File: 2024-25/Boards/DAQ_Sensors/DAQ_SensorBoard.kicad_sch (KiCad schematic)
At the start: 7 parts, among them J1 Conn_01x20_Socket, J2 Conn_01x20_Pin, U1 74LS352, U2 LTC1298CN8-PBF

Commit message: update
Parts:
- added R2, R3: 10k, Resistor_SMD:R_0805_2012Metric_Pad1.20x1.40mm_HandSolder, symbol Device:R_US
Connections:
- net +5V: now also R2.1, R3.1
- net Digital_Temp_Out: now also J1.15 (Pin_15), U1.9 (Zb); no longer J1.11 (Pin_11)
- net GND: now also J1.10 (Pin_10), J1.12 (Pin_12), J1.14 (Pin_14)
- net Pressure1_dig: now also U1.5 (I1a), U1.6 (I0a)
- net Pressure2_dig: now also U1.3 (I3a), U1.4 (I2a)
- net Temp_1+: now reaches R1.2
- net Temp_1+: now also J1.9 (Pin_9)
- net Temp_3+: now reaches J1.13 (Pin_13)
- net Temp_3+: now also R3.2
- net Temp1_dig: now reaches U1.10 (I0b)
- net Temp2_dig: now reaches U1.11 (I1b)
- net Temp3_dig: now reaches U1.12 (I2b)
- new net Temp_2+: J1.11 (Pin_11), R2.2
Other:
- note added: "+5V from battery or powerline?"
- note added: "Selection MUX"

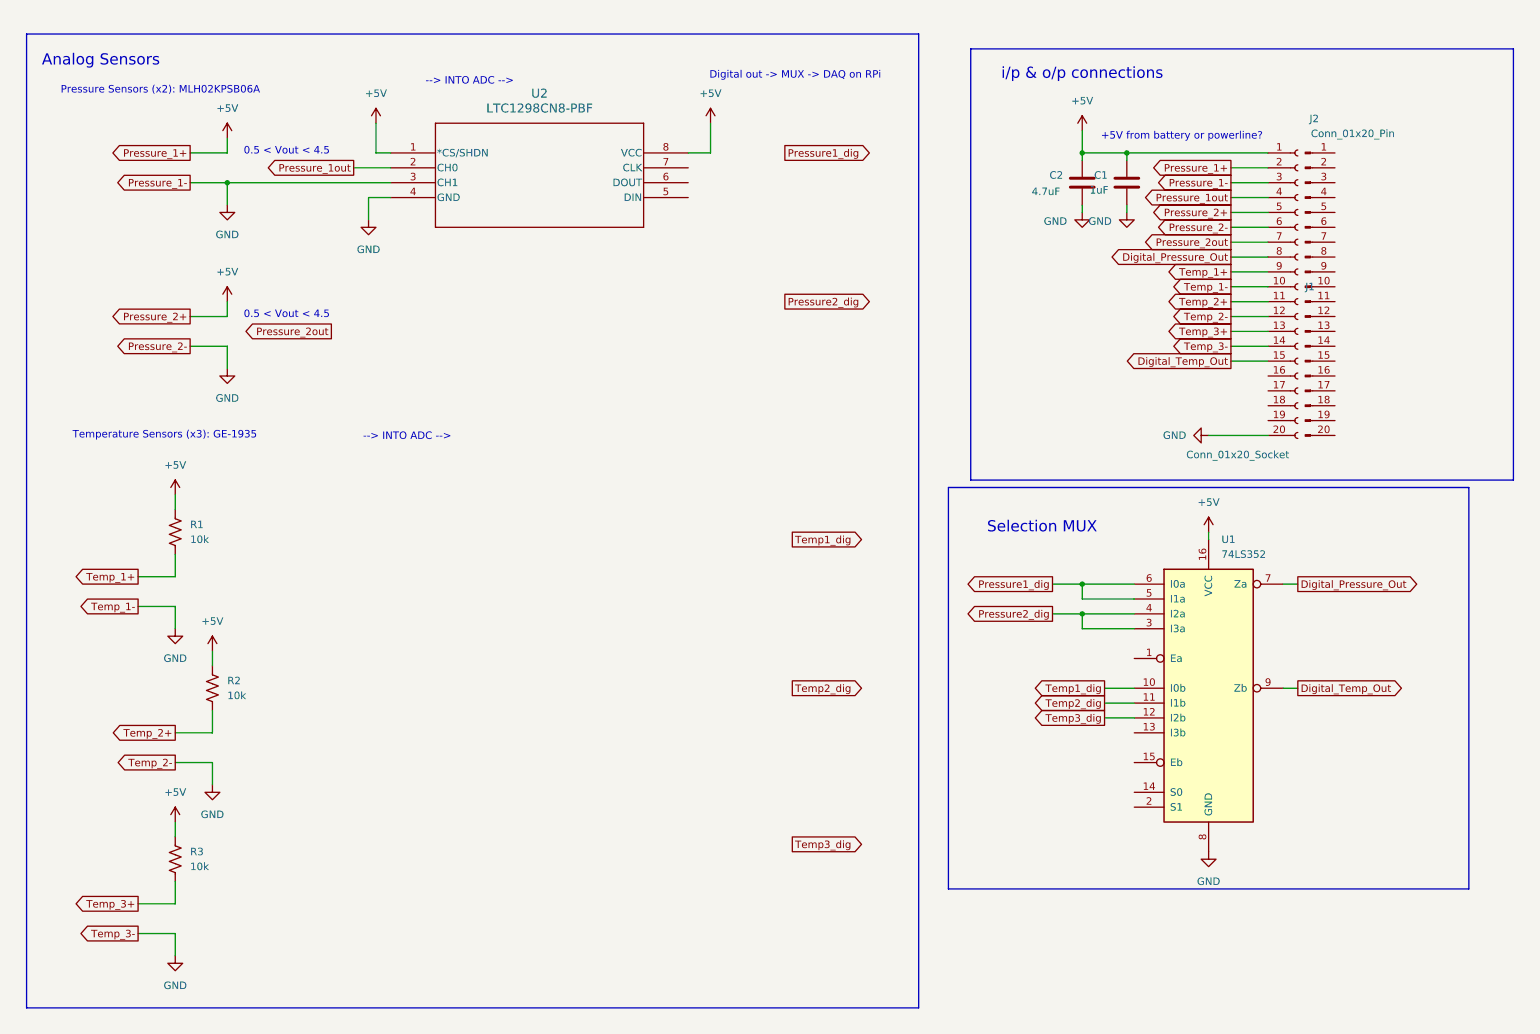
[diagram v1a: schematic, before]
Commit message: changed to 1 ADC with SPI
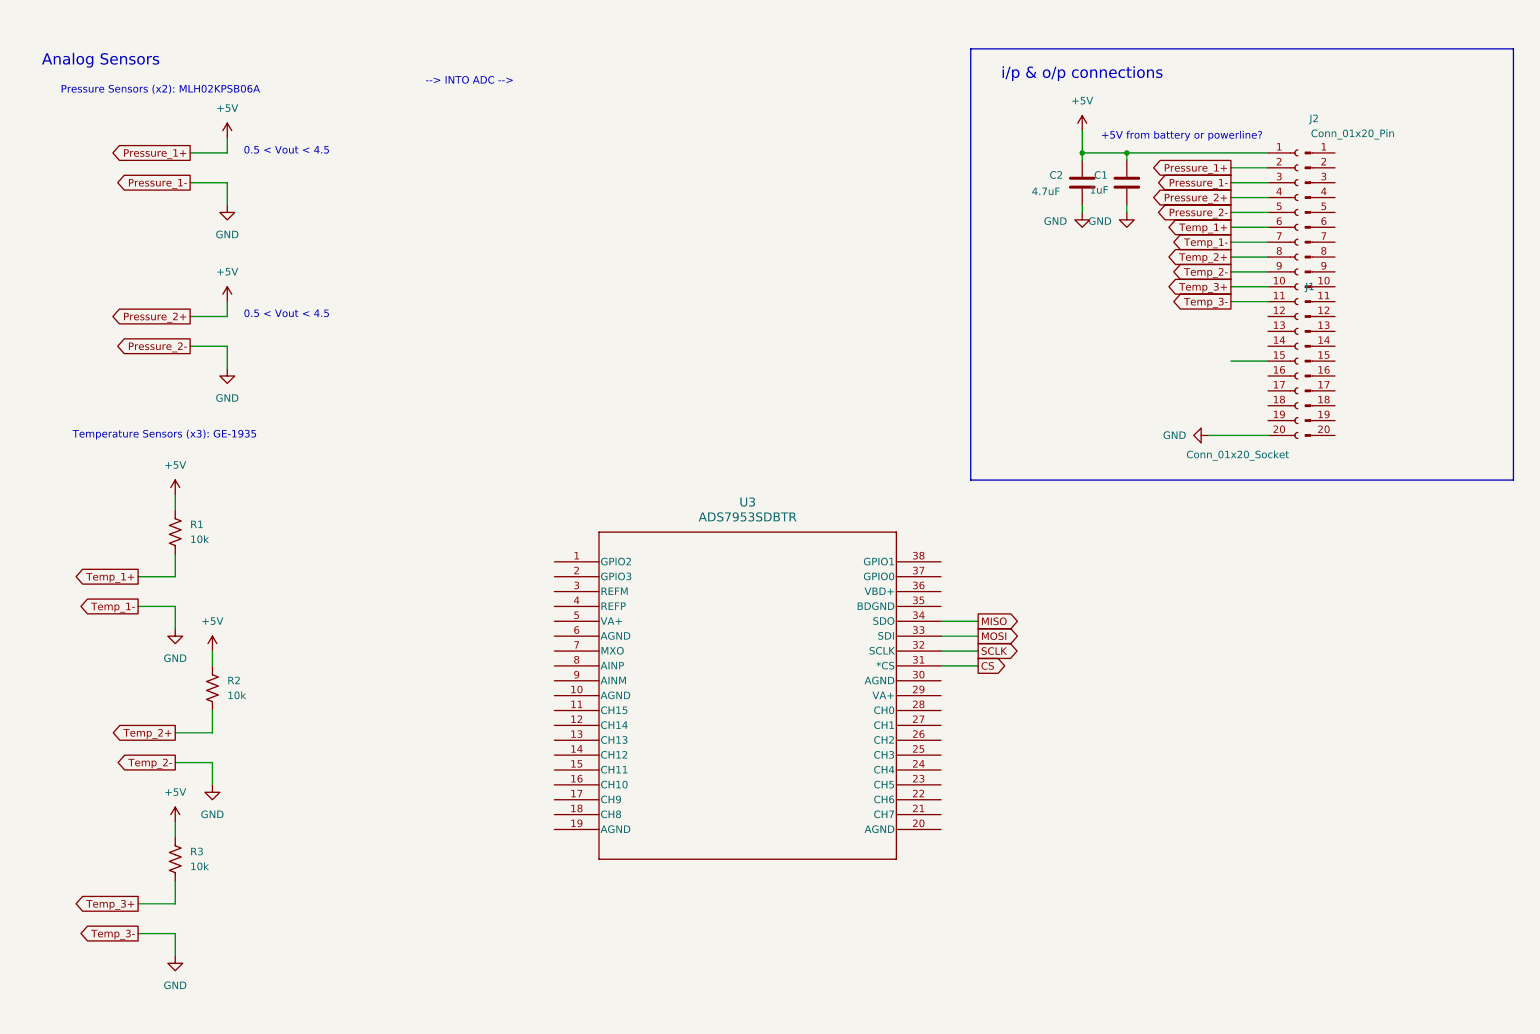
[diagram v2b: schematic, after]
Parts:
- removed U1: 74LS352, symbol 74xx:74LS352
- removed U2: LTC1298CN8-PBF, PDIP-8_N_LIT, symbol LTC1298CN8:LTC1298CN8-PBF
- added U3: ADS7953SDBTR, DBT38, symbol ADS7953SDBTR:ADS7953SDBTR
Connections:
- net Digital_Pressure_Out is gone; now on net Temp_2+: J1.8 (Pin_8)
- net Pressure_1out is gone; now on net +5V: J1.4 (Pin_4)
- net Pressure_2out is gone; now on net GND: J1.7 (Pin_7)
- net +5V: no longer J1.5 (Pin_5)
- net GND: now also J1.11 (Pin_11), J1.5 (Pin_5), J1.9 (Pin_9); no longer J1.10 (Pin_10), J1.12 (Pin_12), J1.14 (Pin_14), J1.6 (Pin_6)
- net Temp_1+: now also J1.6 (Pin_6); no longer J1.9 (Pin_9)
- net Temp_2+: no longer J1.11 (Pin_11)
- net Temp_3+: now also J1.10 (Pin_10); no longer J1.13 (Pin_13)
- net Digital_Temp_Out: no longer names the net of J1.15 (Pin_15)
- new net CS: U3.31 (*CS)
- new net MISO: U3.34 (SDO)
- new net MOSI: U3.33 (SDI)
- new net SCLK: U3.32 (SCLK)
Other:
- note removed: "Digital out -> MUX -> DAQ on RPi"
- note removed: "Selection MUX"

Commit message: completed v1
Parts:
- removed J1: Conn_01x20_Socket, symbol Connector:Conn_01x20_Socket
- removed J2: Conn_01x20_Pin, symbol Connector:Conn_01x20_Pin
- added C3, C4, C5: 1uF, Capacitor_SMD:C_0805_2012Metric_Pad1.18x1.45mm_HandSolder, symbol Device:C
- added J1: Conn_01x24_Pin, symbol Connector:Conn_01x24_Pin
- added J2: Conn_01x24_Socket, symbol Connector:Conn_01x24_Socket
- added TP1: TestPoint, TestPoint:TestPoint_THTPad_2.5x2.5mm_Drill1.2mm, symbol Connector:TestPoint
- added U1, U4: MIC5504-3.3YM5, Package_TO_SOT_SMD:SOT-23-5, symbol Regulator_Linear:MIC5504-3.3YM5
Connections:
- net +5V: now also U3.29 (VA+), U3.5 (VA+), C3.1, C5.1, J2.1 (Pin_1), J2.2 (Pin_2), J2.4 (Pin_4), U1.1 (VIN), U4.1 (VIN)
- net CS: now also J2.17 (Pin_17)
- net GND: now also U3.10 (AGND), U3.19 (AGND), U3.20 (AGND), U3.3 (REFM), U3.30 (AGND), U3.35 (BDGND), U3.6 (AGND), U3.9 (AINM), C3.2, C4.2, C5.2, J2.11 (Pin_11), J2.3 (Pin_3), J2.5 (Pin_5), J2.7 (Pin_7), J2.9 (Pin_9), U1.2 (GND), U4.2 (GND)
- net MISO: now also J2.15 (Pin_15)
- net MOSI: now also J2.14 (Pin_14)
- net SCLK: now also J2.16 (Pin_16)
- net Temp_1+: now also U3.26 (CH2), J2.6 (Pin_6)
- net Temp_2+: now also U3.25 (CH3), J2.8 (Pin_8)
- net Temp_3+: now also U3.24 (CH4), J2.10 (Pin_10)
- net GPIO2: now reaches U3.1 (GPIO2)
- net GPIO2: now also J2.20 (Pin_20)
- net GPIO3: now reaches U3.2 (GPIO3)
- net GPIO3: now also J2.21 (Pin_21)
- net Pressure2_out: now reaches U3.27 (CH1)
- net Pressure2_out: now also J2.13 (Pin_13)
- net Pressure1_out: now reaches U3.28 (CH0)
- net Pressure1_out: now also J2.12 (Pin_12)
- net +3.3V: now reaches U3.36 (VBD+)
- net +3.3V: now also C4.1, U1.5 (VOUT)
- net GPIO0: now reaches U3.37 (GPIO0)
- net GPIO0: now also J2.18 (Pin_18)
- net GPIO1: now reaches U3.38 (GPIO1)
- net GPIO1: now also J2.19 (Pin_19)
- net +2.5V: now reaches U3.4 (REFP)
- net +2.5V: now also U4.5 (VOUT)
- net at U3.7 (MXO): now also U3.8 (AINP), TP1.1
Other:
- note added: "(unsure of where to route enable pins on LDOs)"
- note added: "ADC to Teensy"
- note added: "ADC: Sensor data -> SPI"
- note added: "ENABLE?"
- note added: "Voltage Regulators"
- note added: "from channel mux to ADC"
- note removed: "--> INTO ADC -->"
- moved on the sheet: C1, C2, U3

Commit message: small changes to docu
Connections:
- net +3.3V: now also C5.1, U4.1 (VIN)
- net +5V: no longer C5.1, U4.1 (VIN)
- net GND: now also J2.24 (Pin_24)
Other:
- note added: "ADC (SPI to Teensy)"
- note added: "note: internal enable pulldown in both LDOs"
- note removed: "(unsure of where to route enable pins on LDOs)"
- note removed: "ADC to Teensy"
- note removed: "ENABLE?"
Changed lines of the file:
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@@
 	(wire
 		(pts
+			(xy 220.98 91.44) (xy 234.95 91.44)
+		)
+		(stroke
+			(width 0)
+			(type default)
+		)
+	)
+	(wire
+		(pts
 			(xy 111.76 132.08) (xy 111.76 154.94)
 		)
@@
 		)
 	)
-	(text "(unsure of where to route enable pins on LDOs)"
+	(text "note: internal enable pulldown in both LDOs"
 		(exclude_from_sim no)
-		(at 129.032 26.67 0)
-		(effects
-			(font
-				(size 1.27 1.27)
-			)
-		)
-	)
-	(text "ENABLE?"
-		(exclude_from_sim no)
-		(at 94.234 60.452 0)
+		(at 156.718 81.788 0)
 		(effects
 			(font
@@
 		)
 	)
-	(text "ENABLE?"
-		(exclude_from_sim no)
-		(at 150.114 57.912 0)
-		(effects
-			(font
-				(size 1.27 1.27)
-			)
-		)
-	)
 	(text "Temperature Sensors (x3): GE-1935"
 		(exclude_from_sim no)
@@
 		)
 	)
-	(text "ADC to Teensy"
+	(text "ADC (SPI to Teensy)"
 		(exclude_from_sim no)
 		(at 100.33 92.964 0)
@@
 		(on_board yes)
 		(dnp no)
-		(fields_autoplaced yes)
 		(property "Reference" "J2"
 			(at 241.3 60.9599 0)
@@
 		)
 		(property "Value" "Conn_01x24_Socket"
-			(at 241.3 63.4999 0)
+			(at 249.936 68.834 0)
 			(effects
 				(font
@@
 	(symbol
 		(lib_id "power:GND")
-		(at 207.01 86.36 270)
+		(at 220.98 91.44 270)
 		(unit 1)
 		(exclude_from_sim no)
@@
 		(fields_autoplaced yes)
 		(property "Reference" "#PWR03"
-			(at 200.66 86.36 0)
+			(at 214.63 91.44 0)
 			(effects
 				(font
@@
 		)
 		(property "Value" "GND"
-			(at 203.2 86.3599 90)
+			(at 217.17 91.4399 90)
 			(effects
 				(font
@@
 		)
 		(property "Footprint" ""
-			(at 207.01 86.36 0)
+			(at 220.98 91.44 0)
 			(effects
 				(font
@@
 		)
 		(property "Datasheet" ""
-			(at 207.01 86.36 0)
+			(at 220.98 91.44 0)
 			(effects
 				(font
@@
 		)
 		(property "Description" "Power symbol creates a global label with name \"GND\" , ground"
-			(at 207.01 86.36 0)
+			(at 220.98 91.44 0)
 			(effects
 				(font
@@
 	(symbol
 		(lib_id "power:+3.3V")
-		(at 124.46 53.34 270)
+		(at 86.36 39.37 0)
 		(unit 1)
 		(exclude_from_sim no)
@@
 		(on_board yes)
 		(dnp no)
-		(property "Reference" "#PWR026"
-			(at 120.65 53.34 0)
+		(fields_autoplaced yes)
+		(property "Reference" "#PWR024"
+			(at 86.36 43.18 0)
 			(effects
 				(font
@@
 			)
 		)
-		(property "Value" "+2.5V"
-			(at 122.682 50.546 90)
+		(property "Value" "+3.3V"
+			(at 86.36 34.29 0)
 			(effects
 				(font
 					(size 1.27 1.27)
 				)
-				(justify left)
 			)
 		)
 		(property "Footprint" ""
-			(at 124.46 53.34 0)
+			(at 86.36 39.37 0)
 			(effects
 				(font
@@
 		)
 		(property "Datasheet" ""
-			(at 124.46 53.34 0)
+			(at 86.36 39.37 0)
 			(effects
 				(font
@@
 		)
 		(property "Description" "Power symbol creates a global label with name \"+3.3V\""
-			(at 124.46 53.34 0)
+			(at 86.36 39.37 0)
 			(effects
 				(font
@@
 			(project "DAQ_SensorBoard"
 				(path "/7736ffec-8eeb-486a-9772-0952ff9b5594"
-					(reference "#PWR026")
+					(reference "#PWR024")
 					(unit 1)
 				)
@@
 	)
 	(symbol
-		(lib_id "power:GND")
-		(at 54.61 48.26 0)
+		(lib_id "power:+3.3V")
+		(at 124.46 53.34 270)
 		(unit 1)
 		(exclude_from_sim no)
@@
 		(on_board yes)
 		(dnp no)
-		(fields_autoplaced yes)
-		(property "Reference" "#PWR05"
-			(at 54.61 54.61 0)
+		(property "Reference" "#PWR026"
+			(at 120.65 53.34 0)
 			(effects
 				(font
@@
 			)
 		)
-		(property "Value" "GND"
-			(at 54.61 53.34 0)
+		(property "Value" "+2.5V"
+			(at 122.682 50.546 90)
 			(effects
 				(font
 					(size 1.27 1.27)
 				)
+				(justify left)
 			)
 		)
 		(property "Footprint" ""
-			(at 54.61 48.26 0)
+			(at 124.46 53.34 0)
 			(effects
 				(font
@@
 		)
 		(property "Datasheet" ""
-			(at 54.61 48.26 0)
+			(at 124.46 53.34 0)
 			(effects
 				(font
@@
 			)
 		)
-		(property "Description" "Power symbol creates a global label with name \"GND\" , ground"
-			(at 54.61 48.26 0)
+		(property "Description" "Power symbol creates a global label with name \"+3.3V\""
+			(at 124.46 53.34 0)
 			(effects
 				(font
@@
 		)
 		(instances
-			(project ""
+			(project "DAQ_SensorBoard"
 				(path "/7736ffec-8eeb-486a-9772-0952ff9b5594"
-					(reference "#PWR05")
+					(reference "#PWR026")
 					(unit 1)
 				)
@@
 	)
 	(symbol
-		(lib_id "Device:C")
-		(at 203.2 38.1 0)
+		(lib_id "power:GND")
+		(at 54.61 48.26 0)
 		(unit 1)
 		(exclude_from_sim no)
@@
 		(on_board yes)
 		(dnp no)
-		(property "Reference" "C2"
-			(at 197.612 36.83 0)
+		(fields_autoplaced yes)
+		(property "Reference" "#PWR05"
+			(at 54.61 54.61 0)
 			(effects
 				(font
 					(size 1.27 1.27)
 				)
-				(justify left)
+				(hide yes)
 			)
 		)
-		(property "Value" "4.7uF"
-			(at 194.564 39.624 0)
+		(property "Value" "GND"
+			(at 54.61 53.34 0)
 			(effects
 				(font
 					(size 1.27 1.27)
 				)
-				(justify left)
 			)
 		)
-		(property "Footprint" "Capacitor_SMD:C_0805_2012Metric_Pad1.18x1.45mm_HandSolder"
-			(at 204.1652 41.91 0)
+		(property "Footprint" ""
+			(at 54.61 48.26 0)
 			(effects
 				(font
@@
 			)
 		)
-		(property "Datasheet" "~"
-			(at 203.2 38.1 0)
+		(property "Datasheet" ""
+			(at 54.61 48.26 0)
 			(effects
 				(font
@@
 			)
 		)
-		(property "Description" "Unpolarized capacitor"
-			(at 203.2 38.1 0)
+		(property "Description" "Power symbol creates a global label with name \"GND\" , ground"
+			(at 54.61 48.26 0)
 			(effects
 				(font
@@
 		(pin "1"
 		)
-		(pin "2"
-		)
 		(instances
 			(project ""
 				(path "/7736ffec-8eeb-486a-9772-0952ff9b5594"
-					(reference "C2")
+					(reference "#PWR05")
 					(unit 1)
 				)
@@
 	)
 	(symbol
-		(lib_id "power:+5V")
-		(at 86.36 39.37 0)
+		(lib_id "Device:C")
+		(at 203.2 38.1 0)
 		(unit 1)
 		(exclude_from_sim no)
@@
 		(on_board yes)
 		(dnp no)
-		(fields_autoplaced yes)
-		(property "Reference" "#PWR024"
-			(at 86.36 43.18 0)
+		(property "Reference" "C2"
+			(at 197.612 36.83 0)
 			(effects
 				(font
 					(size 1.27 1.27)
 				)
-				(hide yes)
+				(justify left)
 			)
 		)
-		(property "Value" "+5V"
-			(at 86.36 34.29 0)
+		(property "Value" "4.7uF"
+			(at 194.564 39.624 0)
 			(effects
 				(font
 					(size 1.27 1.27)
 				)
+				(justify left)
 			)
 		)
-		(property "Footprint" ""
-			(at 86.36 39.37 0)
+		(property "Footprint" "Capacitor_SMD:C_0805_2012Metric_Pad1.18x1.45mm_HandSolder"
+			(at 204.1652 41.91 0)
 			(effects
 				(font
@@
 			)
 		)
-		(property "Datasheet" ""
-			(at 86.36 39.37 0)
+		(property "Datasheet" "~"
+			(at 203.2 38.1 0)
 			(effects
 				(font
@@
 			)
 		)
-		(property "Description" "Power symbol creates a global label with name \"+5V\""
-			(at 86.36 39.37 0)
+		(property "Description" "Unpolarized capacitor"
+			(at 203.2 38.1 0)
 			(effects
 				(font
@@
 		(pin "1"
 		)
+		(pin "2"
+		)
 		(instances
-			(project "DAQ_SensorBoard"
+			(project ""
 				(path "/7736ffec-8eeb-486a-9772-0952ff9b5594"
-					(reference "#PWR024")
+					(reference "C2")
 					(unit 1)
 				)
